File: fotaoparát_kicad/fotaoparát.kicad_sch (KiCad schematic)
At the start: 35 parts, among them J1 Conn_01x01_Pin, J10 Conn_01x01_Pin, J11 Conn_01x01_Pin, J12 Conn_01x01_Pin, J2 Conn_01x01_Pin, J3 Conn_01x01_Pin, J4 Conn_01x01_Pin, J5 Conn_01x01_Pin, J6 Conn_01x01_Pin, J7 Conn_01x01_Pin, J8 Conn_01x01_Pin, J9 Conn_01x01_Pin, P1 USB_C_Plug_USB2.0

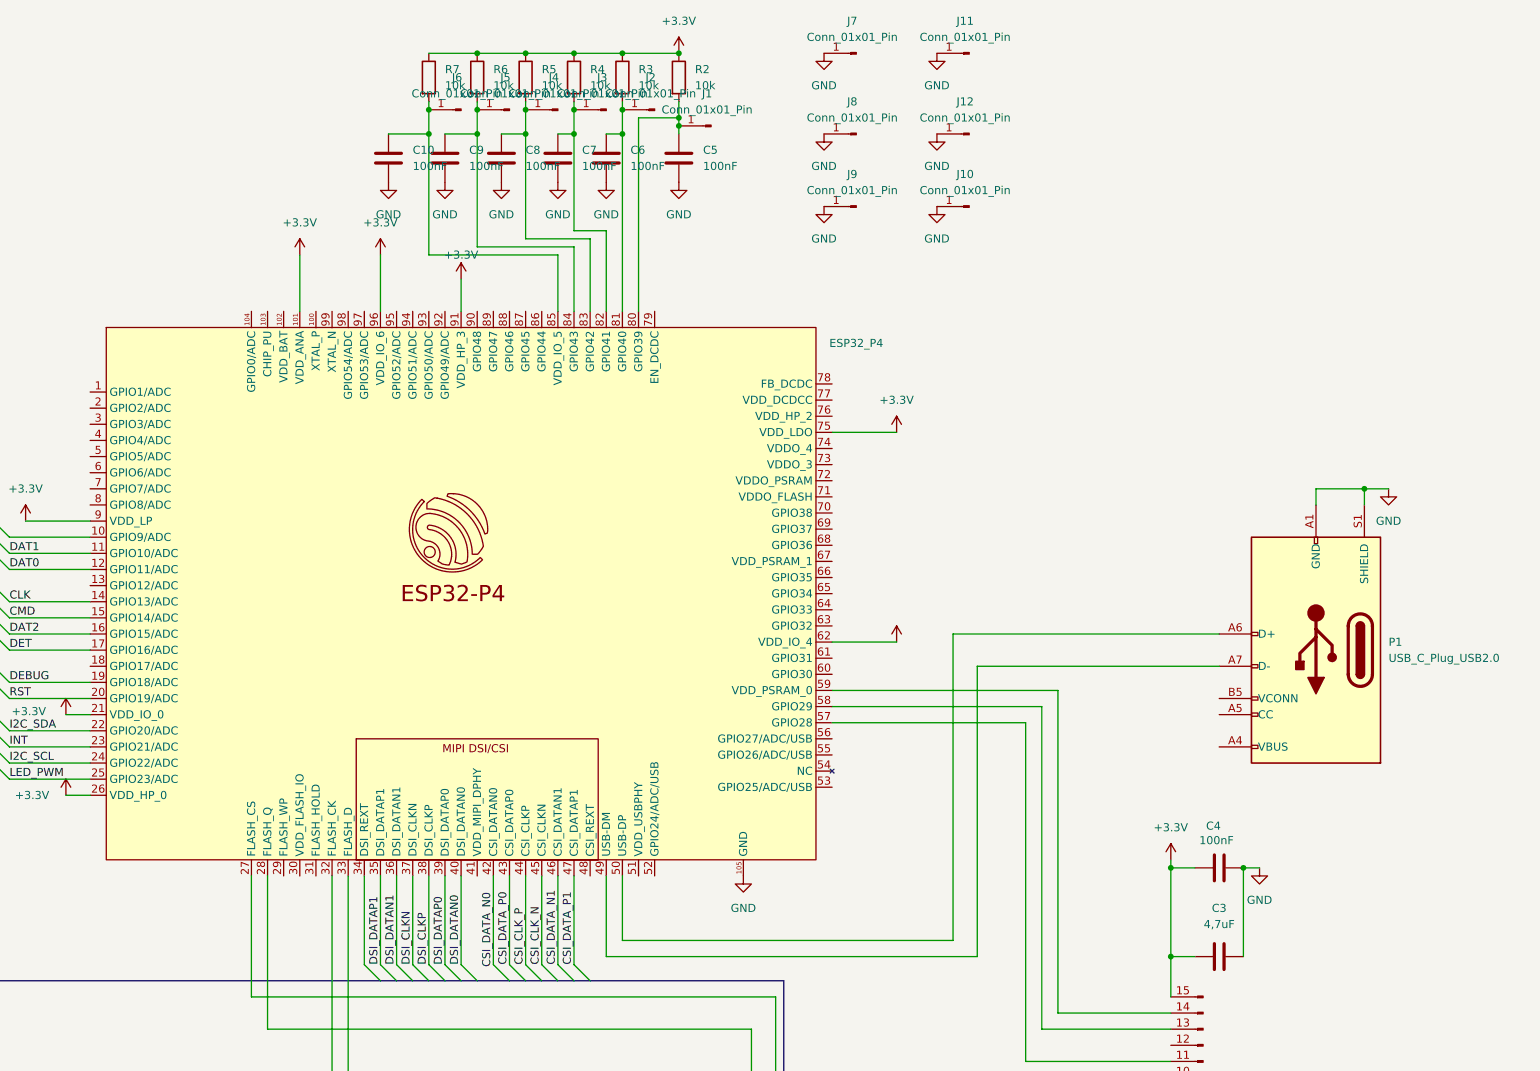
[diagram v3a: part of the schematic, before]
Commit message: Udelani USB-C konektoru, reset a flash tlacitek
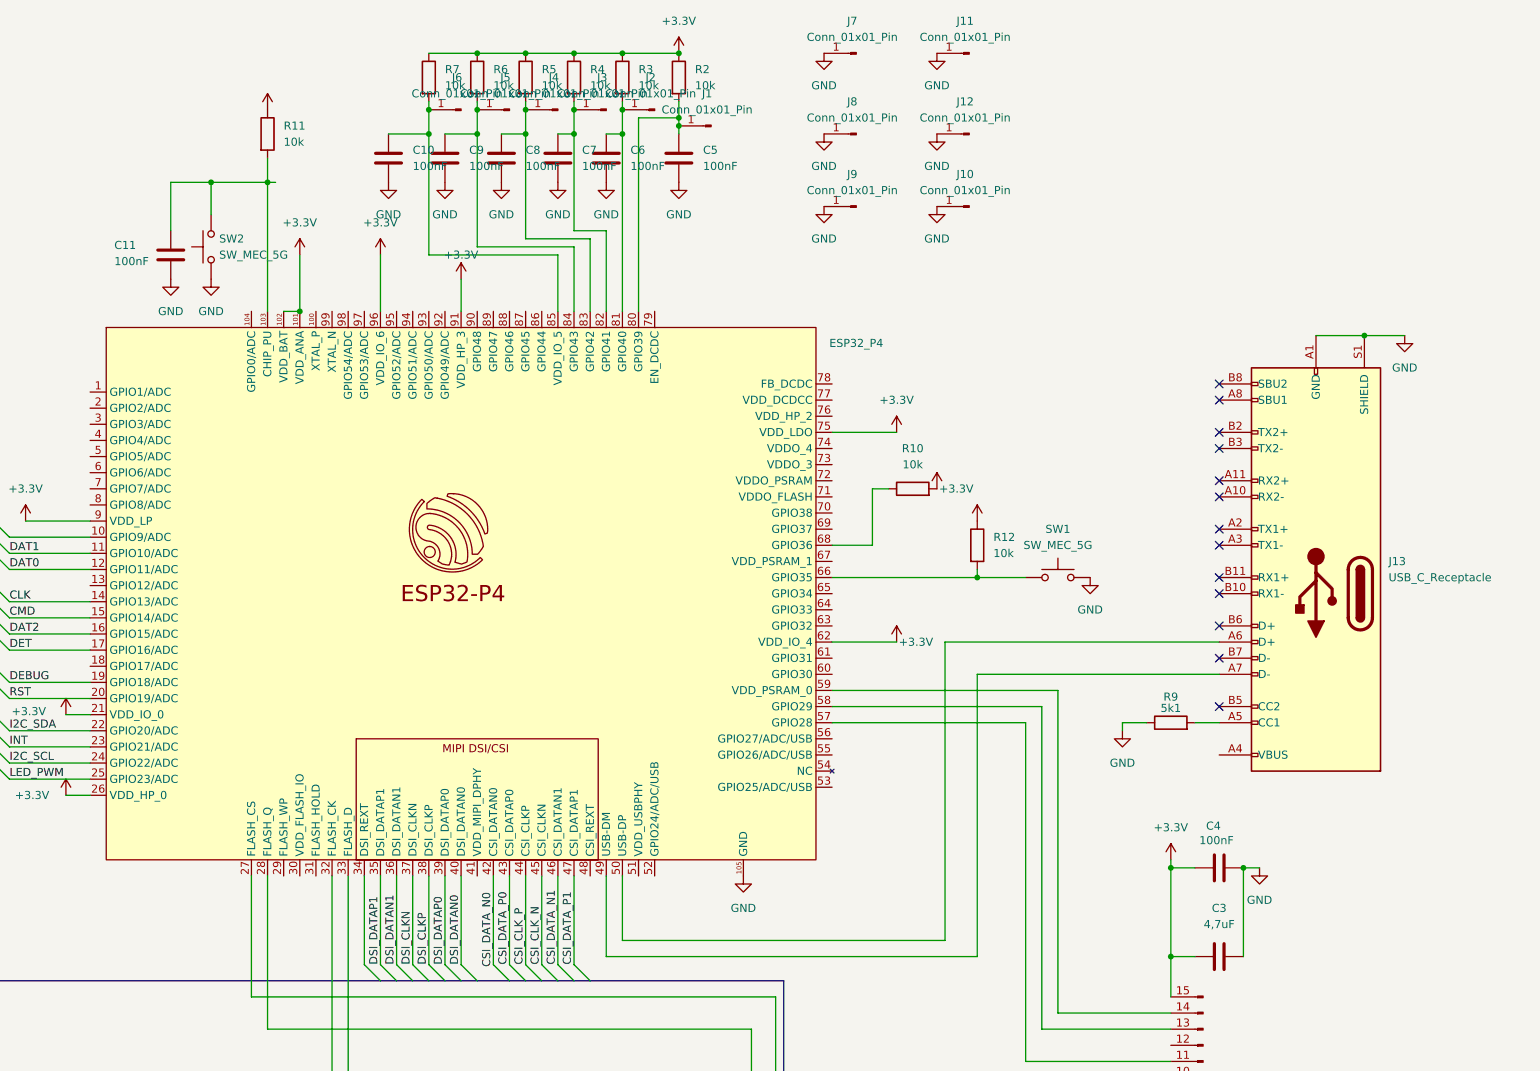
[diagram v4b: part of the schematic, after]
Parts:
- removed P1: USB_C_Plug_USB2.0, Connector_USB:USB_C_Plug_Molex_105444, symbol Connector:USB_C_Plug_USB2.0
- added C11: 100nF, Capacitor_SMD:C_0201_0603Metric, symbol Device:C
- added J13: USB_C_Receptacle, Connector_USB:USB_C_Receptacle_Molex_105450-0101, symbol Connector:USB_C_Receptacle
- added R10, R11, R12: 10k, Resistor_SMD:R_0603_1608Metric, symbol Device:R
- added R9: 5k1, Resistor_SMD:R_0603_1608Metric, symbol Device:R
- added SW1, SW2: SW_MEC_5G, Button_Switch_SMD:SW_MEC_5GSH9, symbol Switch:SW_MEC_5G
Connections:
- net +3.3V: now also ESP32_P4.102 (VDD_BAT), R10.2, R11.1, R12.1
- net GND: now also C11.2, J13.A1 (GND), J13.A12 (GND), J13.B1 (GND), J13.B12 (GND), J13.S1 (SHIELD), R9.1, SW1.3 (B), SW1.4 (B), SW2.1 (A), SW2.2 (A)
- net at ESP32_P4.103 (CHIP_PU): now also C11.1, R11.2, SW2.3 (B), SW2.4 (B)
- net at ESP32_P4.49 (USB-DM): now also J13.A7 (D-)
- net at ESP32_P4.50 (USB-DP): now also J13.A6 (D+)
- net at ESP32_P4.66 (GPIO35): now also R12.2, SW1.1 (A), SW1.2 (A)
- net at ESP32_P4.68 (GPIO36): now also R10.1
- new net: J13.A4 (VBUS), J13.A9 (VBUS), J13.B4 (VBUS), J13.B9 (VBUS)
- new net: J13.A5 (CC1), R9.2
- no-connect marks 0 -> 13

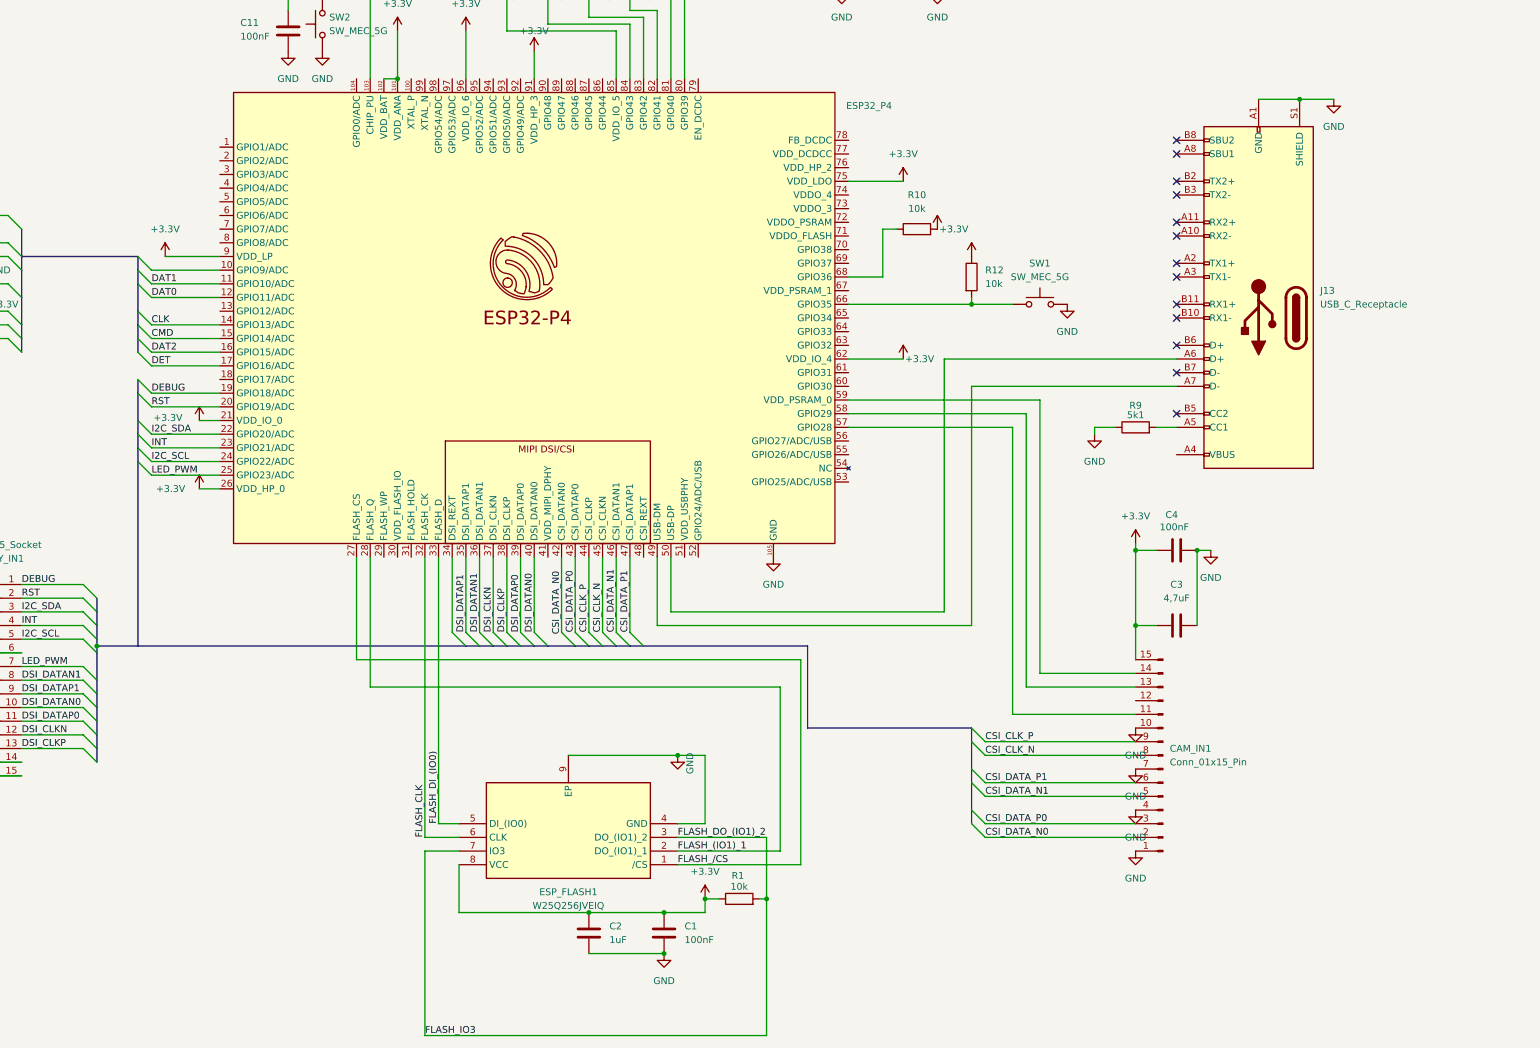
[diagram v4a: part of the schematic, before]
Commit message: Delal jsem znova flash, predelal jsem usb-c konektor a display konektor
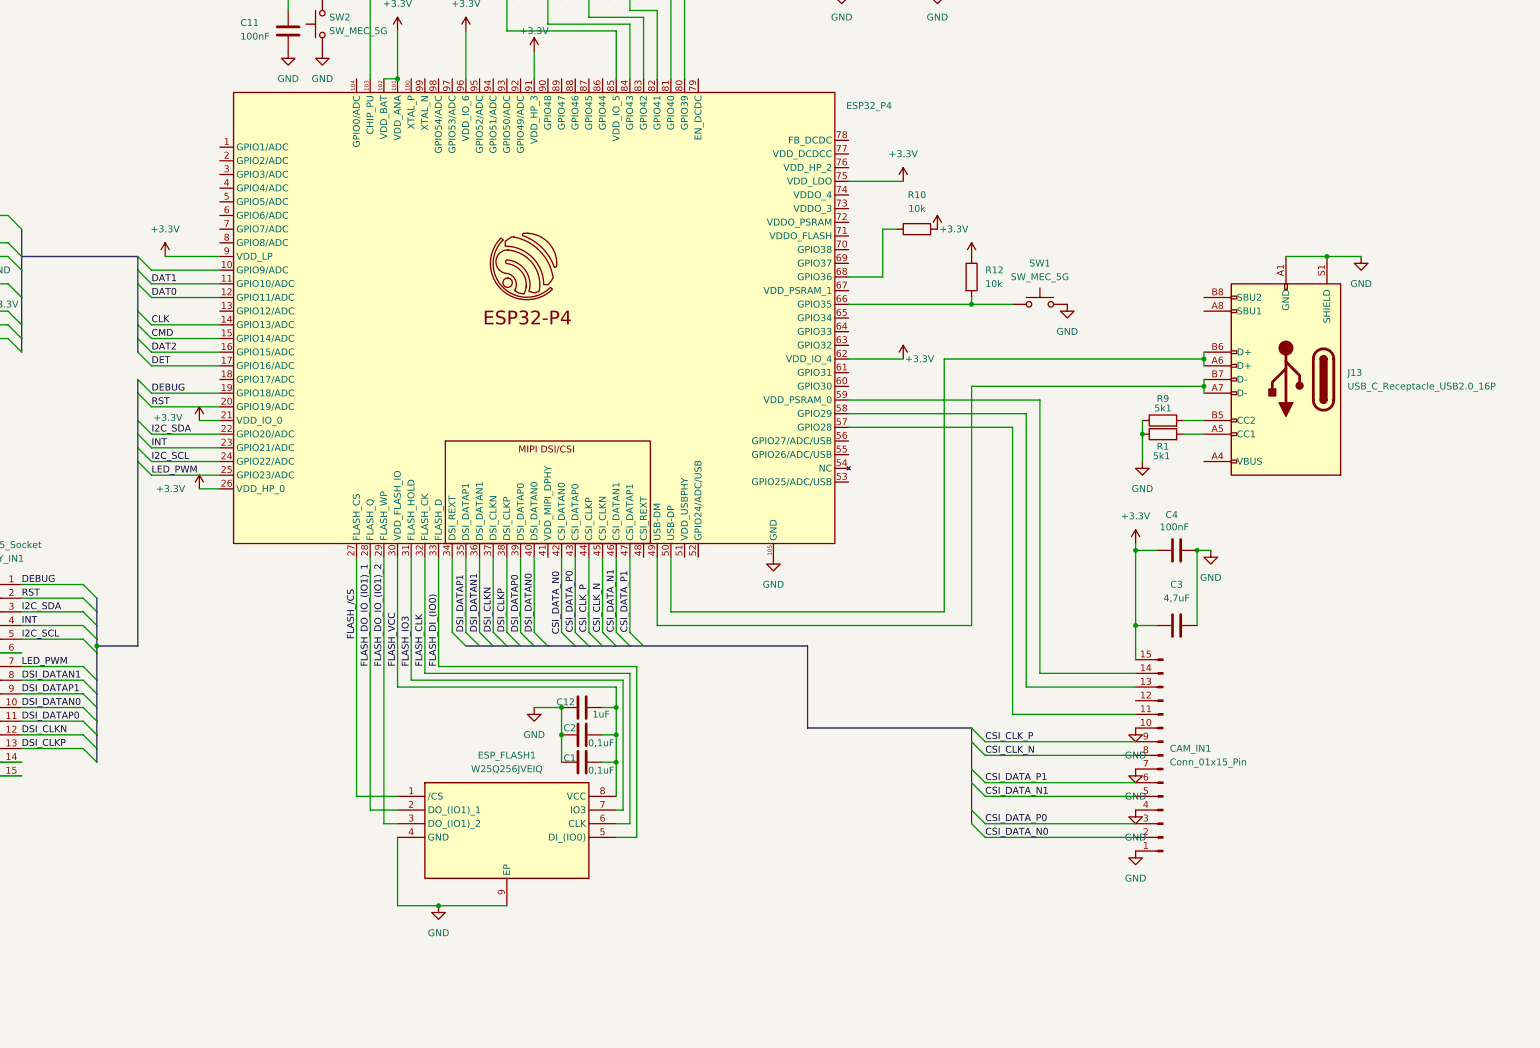
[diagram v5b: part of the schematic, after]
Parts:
- removed J13: USB_C_Receptacle, Connector_USB:USB_C_Receptacle_Molex_105450-0101, symbol Connector:USB_C_Receptacle
- added C12: 1uF, Capacitor_SMD:C_0201_0603Metric, symbol Device:C
- added J13: USB_C_Receptacle_USB2.0_16P, Connector_USB:USB_C_Receptacle_Palconn_UTC16-G, symbol Connector:USB_C_Receptacle_USB2.0_16P
- C1: value 100nF -> 0,1uF
- C2: value 1uF -> 0,1uF
- R1: value 10k -> 5k1
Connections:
- net +3.3V: no longer C1.1, C2.1, ESP_FLASH1.8 (VCC), R1.1
- net GND: now also C1.1, C2.1, R1.1, C12.1, J13.A1 (GND), J13.A12 (GND), J13.B1 (GND), J13.B12 (GND), J13.S1 (SHIELD); no longer C1.2, C2.2
- net at R9.2: now also J13.B5 (CC2)
- net at ESP32_P4.50 (USB-DP): now also J13.A6 (D+), J13.B6 (D+)
- net at ESP32_P4.49 (USB-DM): now also J13.A7 (D-), J13.B7 (D-)
- net FLASH_DO_IO_(IO1)_2: now reaches ESP32_P4.29 (FLASH_WP)
- net FLASH_DO_IO_(IO1)_2: now also ESP_FLASH1.3 (DO_(IO1)_2)
- net FLASH_VCC: now reaches ESP32_P4.30 (VDD_FLASH_IO)
- net FLASH_VCC: now also C1.2, C2.2, ESP_FLASH1.8 (VCC), C12.2
- net FLASH_IO3: now reaches ESP32_P4.31 (FLASH_HOLD)
- net FLASH_IO3: now also ESP_FLASH1.7 (IO3)
- net FLASH_(IO1)_1 renamed FLASH_DO_IO_(IO1)_1
- removed net FLASH_DO_(IO1)_2: ESP_FLASH1.3 (DO_(IO1)_2), ESP_FLASH1.7 (IO3), R1.2
- new net: J13.A4 (VBUS), J13.A9 (VBUS), J13.B4 (VBUS), J13.B9 (VBUS)
- new net: J13.A5 (CC1), R1.2
- no-connect marks 13 -> 0
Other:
- moved on the sheet: ESP_FLASH1, R9
